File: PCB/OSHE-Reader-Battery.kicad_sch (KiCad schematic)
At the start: 15 parts, among them J4 S2B-PH-K-SLFSN, Q1 PNP, U1 BQ2057CSNTR, U2 IRF7326D2TRPBF

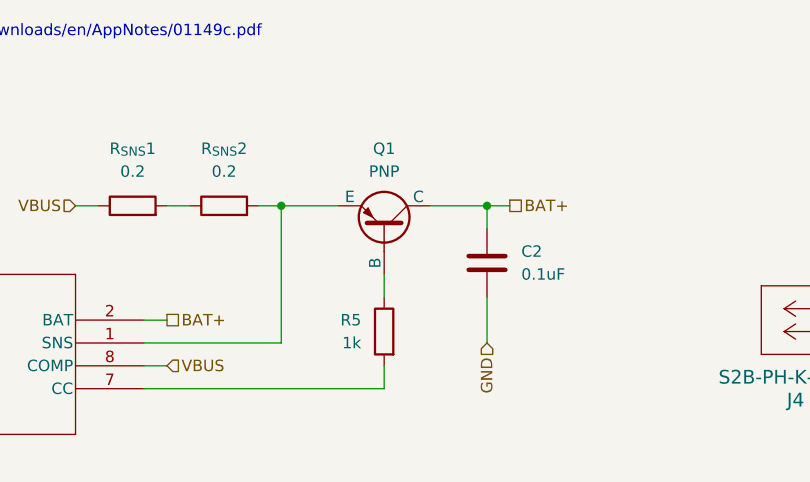
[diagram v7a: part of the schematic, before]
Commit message: Re-did buck converter schematic sheet to more closely resemble TI's datasheet, implemented buck converter on PCB following TI's datasheet layout example
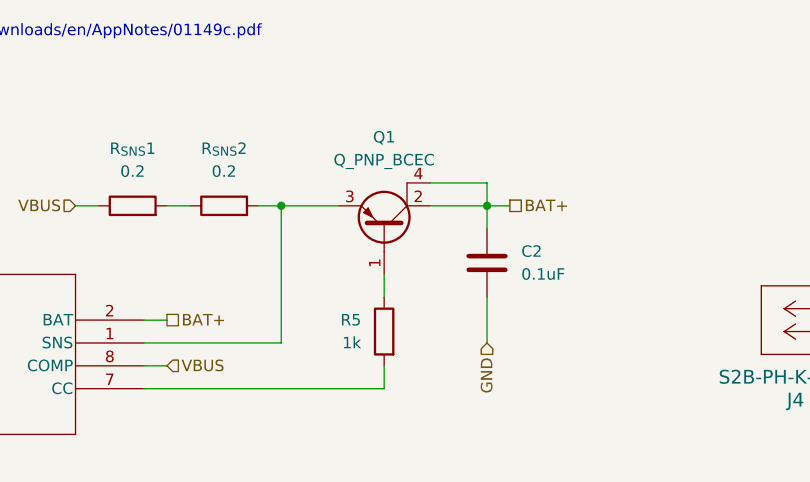
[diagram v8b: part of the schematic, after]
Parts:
- removed Q1: PNP, Package_TO_SOT_THT:TO-92_Inline, symbol Simulation_SPICE:PNP
- added Q1: Q_PNP_BCEC, Package_TO_SOT_SMD:SOT-223, symbol Transistor_BJT:Q_PNP_BCEC
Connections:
- net BAT+: now also Q1.2 (C), Q1.4 (C)
- net at R5.1: now also Q1.1 (B)
- net at R_{SNS}2.2, U1.1 (SNS): now also Q1.3 (E)
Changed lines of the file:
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@@
+	(wire
+		(pts
+			(xy 132.08 43.18) (xy 138.43 43.18)
+		)
+		(stroke
+			(width 0)
+			(type default)
+		)
+	)
+	(wire
+		(pts
+			(xy 138.43 43.18) (xy 138.43 45.72)
+		)
+		(stroke
+			(width 0)
+			(type default)
+		)
+	)
 	(wire
 		(pts
@@
 			)
 			(justify left)
+		)
+	)
+	(symbol
+		(lib_id "Transistor_BJT:Q_PNP_BCEC")
+		(at 127 48.26 270)
+		(mirror x)
+		(unit 1)
+		(exclude_from_sim no)
+		(in_bom yes)
+		(on_board yes)
+		(dnp no)
+		(fields_autoplaced yes)
+		(property "Reference" "Q1"
+			(at 127 38.1 90)
+			(effects
+				(font
+					(size 1.27 1.27)
+				)
+			)
+		)
+		(property "Value" "Q_PNP_BCEC"
+			(at 127 40.64 90)
+			(effects
+				(font
+					(size 1.27 1.27)
+				)
+			)
+		)
+		(property "Footprint" "Package_TO_SOT_SMD:SOT-223"
+			(at 129.54 43.18 0)
+			(effects
+				(font
+					(size 1.27 1.27)
+				)
+				(hide yes)
+			)
+		)
+		(property "Datasheet" "~"
+			(at 127 48.26 0)
+			(effects
+				(font
+					(size 1.27 1.27)
+				)
+				(hide yes)
+			)
+		)
+		(property "Description" "PNP transistor, base/collector/emitter, collector connected to mounting plane"
+			(at 127 48.26 0)
+			(effects
+				(font
+					(size 1.27 1.27)
+				)
+				(hide yes)
+			)
+		)
+		(pin "4"
+		)
+		(pin "2"
+		)
+		(pin "1"
+		)
+		(pin "3"
+		)
+		(instances
+			(project ""
+				(path "/3f072c92-e35a-4654-839b-728bd3dc3a46/9b683008-b3f5-4049-bcf9-7e8cdd298ddd"
+					(reference "Q1")
+					(unit 1)
+				)
+			)
 		)
 	)
@@
 					(unit 1)
 				)
-			)
-		)
-	)
-	(symbol
-		(lib_id "Simulation_SPICE:PNP")
-		(at 127 48.26 270)
-		(mirror x)
-		(unit 1)
-		(exclude_from_sim no)
-		(in_bom yes)
-		(on_board yes)
-		(dnp no)
-		(property "Reference" "Q1"
-			(at 127 39.37 90)
-			(effects
-				(font
-					(size 1.27 1.27)
-				)
-			)
-		)
-		(property "Value" "PNP"
-			(at 127 41.91 90)
-			(effects
-				(font
-					(size 1.27 1.27)
-				)
-			)
-		)
-		(property "Footprint" "Package_TO_SOT_THT:TO-92_Inline"
-			(at 127 12.7 0)
-			(effects
-				(font
-					(size 1.27 1.27)
-				)
-				(hide yes)
-			)
-		)
-		(property "Datasheet" "https://ngspice.sourceforge.io/docs/ngspice-html-manual/manual.xhtml#cha_BJTs"
-			(at 127 12.7 0)
-			(effects
-				(font
-					(size 1.27 1.27)
-				)
-				(hide yes)
-			)
-		)
-		(property "Description" "Bipolar transistor symbol for simulation only, substrate tied to the emitter"
-			(at 127 48.26 0)
-			(effects
-				(font
-					(size 1.27 1.27)
-				)
-				(hide yes)
-			)
-		)
-		(property "Sim.Device" "PNP"
-			(at 127 48.26 0)
-			(effects
-				(font
-					(size 1.27 1.27)
-				)
-				(hide yes)
-			)
-		)
-		(property "Sim.Type" "GUMMELPOON"
-			(at 127 48.26 0)
-			(effects
-				(font
-					(size 1.27 1.27)
-				)
-				(hide yes)
-			)
-		)
-		(property "Sim.Pins" "1=C 2=B 3=E"
-			(at 127 48.26 0)
-			(effects
-				(font
-					(size 1.27 1.27)
-				)
-				(hide yes)
-			)
-		)
-		(pin "3"
-		)
-		(pin "1"
-		)
-		(pin "2"
-		)
-		(instances
-			(project "OSHE-Reader-Battery"
-				(path "/0e6b7f01-01db-4a40-bfc7-232b1ad59e06"
-					(reference "Q1")
-					(unit 1)
-				)
-			)
-			(project "OSHE-Reader-PCB"
-				(path "/3f072c92-e35a-4654-839b-728bd3dc3a46/9b683008-b3f5-4049-bcf9-7e8cdd298ddd"
-					(reference "Q1")
-					(unit 1)
-				)
